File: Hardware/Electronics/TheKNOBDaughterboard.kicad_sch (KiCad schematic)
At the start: 52 parts, among them J1 Conn_01x02_Female, J2 USB_C_Receptacle_USB2.0, J3 Conn_01x03, J4 Conn_01x04, J5 Conn_01x11, Q1 Q_NMOS_GSD, Q2 Q_NMOS_GSD, SW1 SW_Push, SW2 SW_Push, U1 MCP73831-5-OT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

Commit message: add 3d files, changes to sch and pcb
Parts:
- J1: footprint Connector_JST:JST_GH_BM02B-GHS-TBT_1x02-1MP_P1.25mm_Vertical -> Connector_JST:JST_PH_S2B-PH-SM4-TB_1x02-1MP_P2.00mm_Horizontal

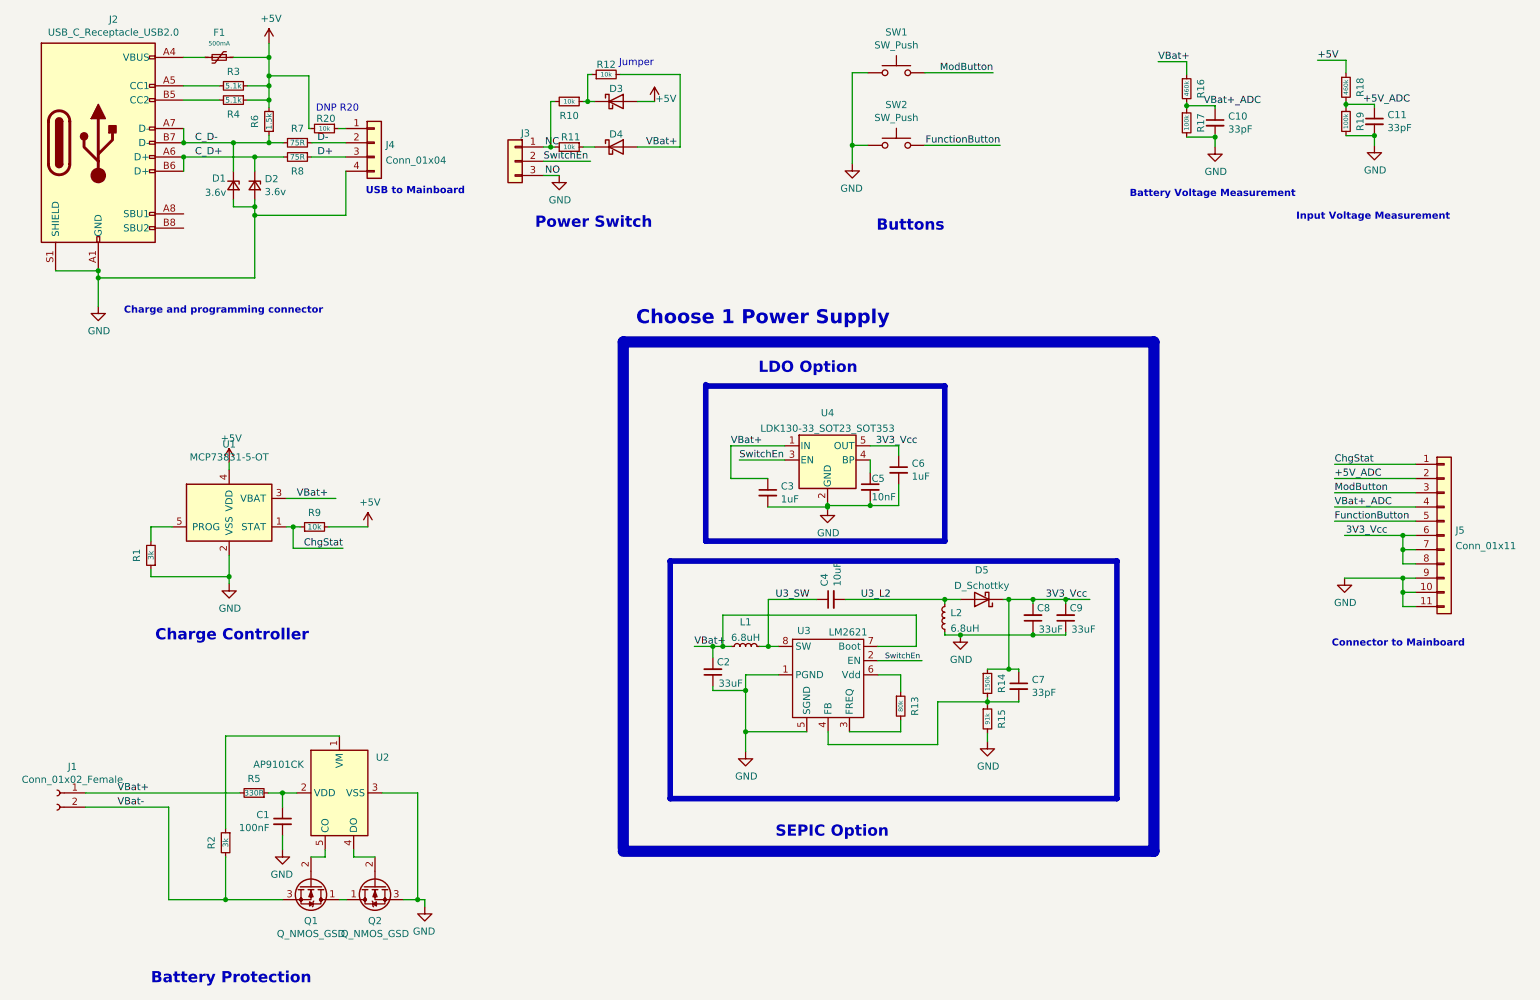
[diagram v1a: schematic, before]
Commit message: Batt Protection and SMPS chip changed due to chip shortage
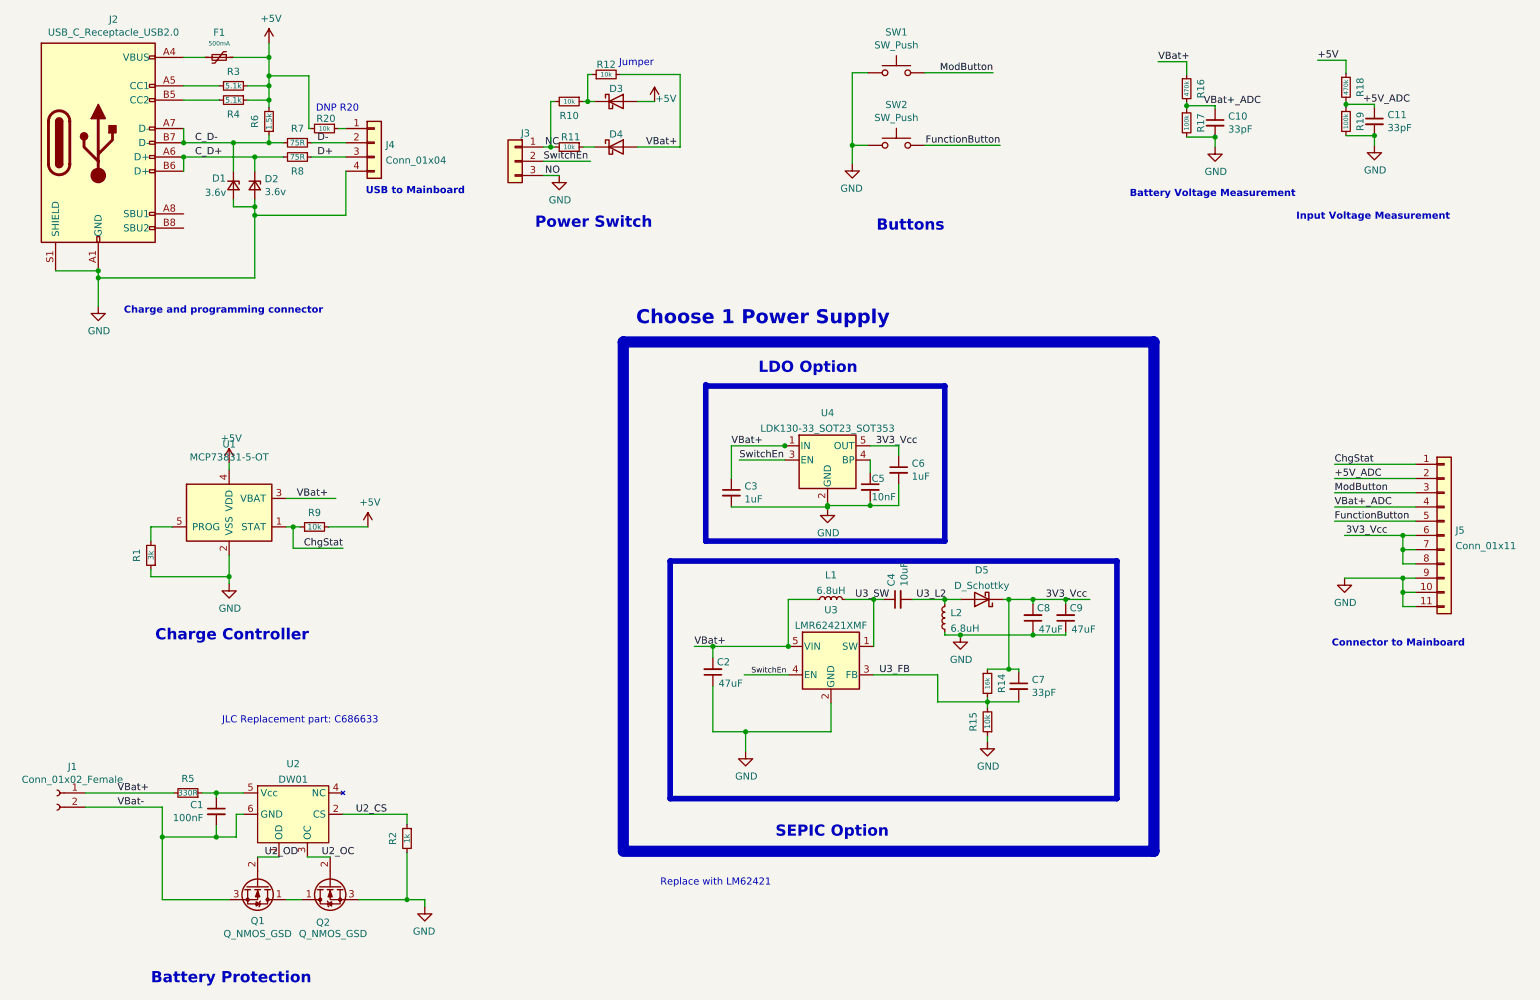
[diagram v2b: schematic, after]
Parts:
- removed R13: 80k, Resistor_SMD:R_0603_1608Metric, symbol Device:R_Small
- removed U2: AP9101CK, Package_TO_SOT_SMD:SOT-23-5, symbol Battery_Management:AP9101CK
- removed U3: LM2621, Package_SO:VSSOP-8_3.0x3.0mm_P0.65mm, symbol TheKnobSymbolLibrary:LM2621
- added U2: DW01, Package_TO_SOT_SMD:SOT-23-6, symbol TheKnobLib:DW01
- added U3: LMR62421XMF, Package_TO_SOT_SMD:SOT-23-5, symbol Regulator_Switching:LMR62421XMF
- C2, C8, C9: value 33uF -> 47uF
- R14: value 150k -> 16k
- R15: value 91k -> 10k
- R16, R18: value 460k -> 470k
- R2: value 3k -> 1k
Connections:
- net GND: now also R15.1, R2.2, U3.2 (GND); no longer C1.2, R15.2
- net SwitchEn: now also U3.4 (EN)
- net U3_SW: now also U3.1 (SW)
- net VBat+: now also U3.5 (VIN)
- net VBat-: now also C1.2, U2.6 (GND); no longer R2.2
- net U2_CS: now reaches R2.1
- net U2_CS: now also U2.2 (CS)
- net at C1.1, R5.1: now also U2.5 (Vcc)
- net U2_OC: now reaches Q2.2 (G)
- net U2_OC: now also U2.3 (OC)
- net U2_OD: now reaches Q1.2 (G)
- net U2_OD: now also U2.1 (OD)
- net U3_FB: now reaches C7.2, R14.2
- net U3_FB: now also R15.2, U3.3 (FB); no longer R15.1
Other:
- note added: "JLC Replacement part: C686633"
- note added: "Replace with LM62421"
- moved on the sheet: C1, C3, C4, L1, Q1, Q2, R2, R5
